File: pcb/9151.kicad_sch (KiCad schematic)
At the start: 17 parts, among them J1 SIM_Card, J5 Conn_ARM_SWD_TagConnect_TC203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, U1 nRF9151-LAXX, U3 W25Q128JVP

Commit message: Clean up sch
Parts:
- removed L1: L_Ferrite, symbol Device:L_Ferrite
- added C38: 0.1u, symbol Device:C
- added FB1: FerriteBead, symbol Device:FerriteBead
- added J9: Conn_Coaxial, symbol Connector:Conn_Coaxial
- added R7, R8: 10k, symbol Device:R
- C1, C2, C5, C6: value C -> 0.1u
- C3: value C -> 15p
- C4: value C -> 47u
- C7, C8: value C -> 4.7u
- R1: value R -> 10k
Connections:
- net +3V3: now also R7.1, R8.1; no longer R1.1
- net GND: now also C38.2, J9.2 (Ext)
- net SCL: now also R7.2
- net SDA: now also R8.2
- net SIM_1V8: now also C38.1
- net V_9151: now also C3.1, FB1.1
- net at C2.1, U1.14 (VDD): now also R1.1, FB1.2; no longer C3.1
- net RF: now reaches U1.35 (ANT)
- net RF: now also J9.1 (In)
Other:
- note added: "Flash"
- note added: "I2C"
- note added: "SWD"
- note added: "TODO: Can internal pullups do this?"
- note added: "nRF9151"
- moved on the sheet: C1, C2, C25, C3, C4, C6, C7, C8, J1, J5, R1, R5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

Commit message: Footprints
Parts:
- C1, C2, C25, C3, C38, C5, C6: footprint (none) -> Capacitor_SMD:C_0603_1608Metric
- C4, C7, C8: footprint (none) -> Capacitor_SMD:C_0805_2012Metric
- FB1: footprint (none) -> Inductor_SMD:L_0603_1608Metric
- J1: footprint (none) -> Connector_Card:nanoSIM_GCT_SIM8060-6-0-14-00
- J9: footprint (none) -> Connector_Coaxial:U.FL_Molex_MCRF_73412-0110_Vertical
- R1, R5, R6, R7, R8: footprint (none) -> Resistor_SMD:R_0603_1608Metric
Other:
- note added: "Internal pull-ups are good to 100kHz"
- note removed: "TODO: Can internal pullups do this?"
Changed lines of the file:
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@@
 		)
 	)
-	(text "Flash"
+	(text "Internal pull-ups \nare good to 100kHz"
 		(exclude_from_sim no)
-		(at 239.014 16.764 0)
+		(at 203.708 151.13 0)
 		(effects
 			(font
-				(size 1.778 1.778)
-				(thickness 0.254)
-				(bold yes)
-				(color 0 11 255 1)
+				(size 1.27 1.27)
+				(color 3 0 255 1)
 			)
 		)
 	)
-	(text "TODO: Can internal \npullups do this?"
+	(text "Flash"
 		(exclude_from_sim no)
-		(at 200.914 150.622 0)
+		(at 239.014 16.764 0)
 		(effects
 			(font
-				(size 1.27 1.27)
+				(size 1.778 1.778)
 				(thickness 0.254)
 				(bold yes)
-				(color 255 0 248 1)
+				(color 0 11 255 1)
 			)
 		)
@@
 			(font
 				(size 1.27 1.27)
-				(color 255 0 235 1)
+				(color 7 0 255 1)
 			)
 		)
@@
 			)
 		)
-		(property "Footprint" ""
+		(property "Footprint" "Capacitor_SMD:C_0603_1608Metric"
 			(at 155.9052 163.83 0)
 			(effects
@@
 			)
 		)
-		(property "Footprint" ""
+		(property "Footprint" "Resistor_SMD:R_0603_1608Metric"
 			(at 212.852 135.89 90)
 			(effects
@@
 			)
 		)
-		(property "Footprint" ""
+		(property "Footprint" "Capacitor_SMD:C_0805_2012Metric"
 			(at 141.9352 35.56 0)
 			(effects
@@
 			)
 		)
-		(property "Footprint" ""
+		(property "Footprint" "Capacitor_SMD:C_0603_1608Metric"
 			(at 254.9652 54.61 0)
 			(effects
@@
 			)
 		)
-		(property "Footprint" ""
+		(property "Footprint" "Capacitor_SMD:C_0603_1608Metric"
 			(at 116.5352 38.1 0)
 			(effects
@@
 			)
 		)
-		(property "Footprint" ""
+		(property "Footprint" "Capacitor_SMD:C_0805_2012Metric"
 			(at 141.9352 64.77 0)
 			(effects
@@
 			)
 		)
-		(property "Footprint" ""
+		(property "Footprint" "Inductor_SMD:L_0603_1608Metric"
 			(at 67.31 28.448 90)
 			(effects
@@
 			)
 		)
-		(property "Footprint" ""
+		(property "Footprint" "Resistor_SMD:R_0603_1608Metric"
 			(at 193.802 135.89 90)
 			(effects
@@
 			)
 		)
-		(property "Footprint" ""
+		(property "Footprint" "Capacitor_SMD:C_0603_1608Metric"
 			(at 91.1352 35.56 0)
 			(effects
@@
 			)
 		)
-		(property "Footprint" ""
+		(property "Footprint" "Resistor_SMD:R_0603_1608Metric"
 			(at 73.152 33.02 90)
 			(effects
@@
 			)
 		)
-		(property "Footprint" ""
+		(property "Footprint" "Resistor_SMD:R_0603_1608Metric"
 			(at 205.232 46.99 90)
 			(effects
@@
 			)
 		)
-		(property "Footprint" ""
+		(property "Footprint" "Connector_Card:nanoSIM_GCT_SIM8060-6-0-14-00"
 			(at 41.91 165.1 0)
 			(effects
@@
 			)
 		)
-		(property "Footprint" ""
+		(property "Footprint" "Capacitor_SMD:C_0603_1608Metric"
 			(at 59.3852 35.56 0)
 			(effects
@@
 			)
 		)
-		(property "Footprint" ""
+		(property "Footprint" "Capacitor_SMD:C_0805_2012Metric"
 			(at 35.2552 35.56 0)
 			(effects
@@
 			)
 		)
-		(property "Footprint" ""
+		(property "Footprint" "Capacitor_SMD:C_0603_1608Metric"
 			(at 46.6852 35.56 0)
 			(effects
@@
 			)
 		)
-		(property "Footprint" ""
+		(property "Footprint" "Resistor_SMD:R_0603_1608Metric"
 			(at 209.042 46.99 90)
 			(effects
@@
 			)
 		)
-		(property "Footprint" ""
+		(property "Footprint" "Capacitor_SMD:C_0603_1608Metric"
 			(at 130.5052 35.56 0)
 			(effects
@@
 			)
 		)
-		(property "Footprint" ""
+		(property "Footprint" "Connector_Coaxial:U.FL_Molex_MCRF_73412-0110_Vertical"
 			(at 151.13 76.2 0)
 			(effects

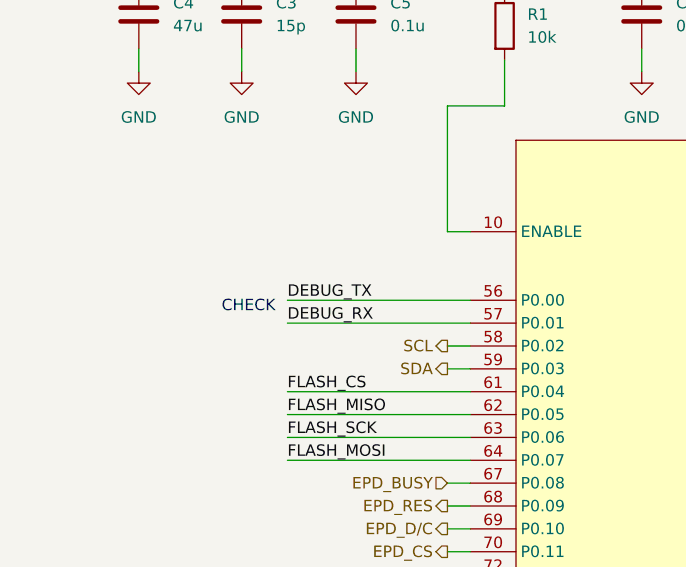
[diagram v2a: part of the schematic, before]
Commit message: ERC errors
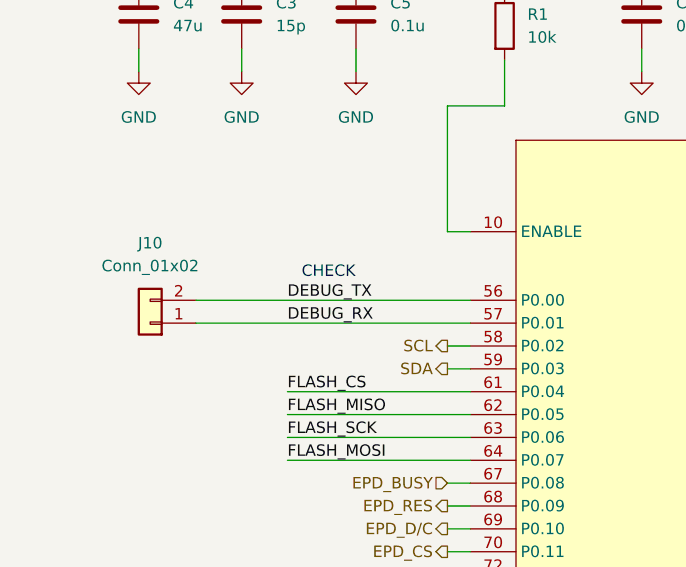
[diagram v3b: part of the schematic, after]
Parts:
- added J10: Conn_01x02, symbol Connector_Generic:Conn_01x02
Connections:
- net DEBUG_RX: now also J10.1 (Pin_1)
- net DEBUG_TX: now also J10.2 (Pin_2)
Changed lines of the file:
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@@
 	(text "CHECK"
 		(exclude_from_sim no)
-		(at 46.482 64.262 0)
+		(at 55.372 60.452 0)
 		(effects
 			(font
@@
 	(wire
 		(pts
-			(xy 50.8 63.5) (xy 71.12 63.5)
+			(xy 207.01 62.23) (xy 228.6 62.23)
 		)
 		(stroke
@@
 	(wire
 		(pts
-			(xy 207.01 62.23) (xy 228.6 62.23)
+			(xy 58.42 35.56) (xy 58.42 38.1)
 		)
 		(stroke
@@
 	(wire
 		(pts
-			(xy 68.58 129.54) (xy 71.12 129.54)
+			(xy 40.64 66.04) (xy 71.12 66.04)
 		)
 		(stroke
@@
 	(wire
 		(pts
-			(xy 256.54 146.05) (xy 256.54 148.59)
+			(xy 40.64 63.5) (xy 71.12 63.5)
 		)
 		(stroke
@@
 	(wire
 		(pts
-			(xy 137.16 154.94) (xy 154.94 154.94)
+			(xy 68.58 129.54) (xy 71.12 129.54)
 		)
 		(stroke
@@
 	(wire
 		(pts
-			(xy 74.93 26.67) (xy 90.17 26.67)
+			(xy 256.54 146.05) (xy 256.54 148.59)
 		)
 		(stroke
@@
 	(wire
 		(pts
-			(xy 256.54 118.11) (xy 256.54 125.73)
+			(xy 137.16 154.94) (xy 154.94 154.94)
 		)
 		(stroke
@@
 	(wire
 		(pts
-			(xy 266.7 138.43) (xy 274.32 138.43)
+			(xy 74.93 26.67) (xy 90.17 26.67)
 		)
 		(stroke
@@
 	(wire
 		(pts
-			(xy 140.97 64.77) (xy 140.97 66.04)
+			(xy 256.54 118.11) (xy 256.54 125.73)
 		)
 		(stroke
@@
 	(wire
 		(pts
-			(xy 34.29 35.56) (xy 34.29 38.1)
+			(xy 266.7 138.43) (xy 274.32 138.43)
 		)
 		(stroke
@@
 	(wire
 		(pts
-			(xy 137.16 160.02) (xy 144.78 160.02)
+			(xy 140.97 64.77) (xy 140.97 66.04)
 		)
 		(stroke
@@
 	(wire
 		(pts
-			(xy 58.42 35.56) (xy 58.42 38.1)
+			(xy 34.29 35.56) (xy 34.29 38.1)
 		)
 		(stroke
@@
 	(wire
 		(pts
-			(xy 50.8 66.04) (xy 71.12 66.04)
+			(xy 137.16 160.02) (xy 144.78 160.02)
 		)
 		(stroke
@@
 					(unit 1)
 				)
+			)
+		)
+	)
+	(symbol
+		(lib_id "Connector_Generic:Conn_01x02")
+		(at 35.56 66.04 180)
+		(unit 1)
+		(exclude_from_sim no)
+		(in_bom yes)
+		(on_board yes)
+		(dnp no)
+		(fields_autoplaced yes)
+		(property "Reference" "J10"
+			(at 35.56 57.15 0)
+			(effects
+				(font
+					(size 1.27 1.27)
+				)
+			)
+		)
+		(property "Value" "Conn_01x02"
+			(at 35.56 59.69 0)
+			(effects
+				(font
+					(size 1.27 1.27)
+				)
+			)
+		)
+		(property "Footprint" ""
+			(at 35.56 66.04 0)
+			(effects
+				(font
+					(size 1.27 1.27)
+				)
+				(hide yes)
+			)
+		)
+		(property "Datasheet" "~"
+			(at 35.56 66.04 0)
+			(effects
+				(font
+					(size 1.27 1.27)
+				)
+				(hide yes)
+			)
+		)
+		(property "Description" "Generic connector, single row, 01x02, script generated (kicad-library-utils/schlib/autogen/connector/)"
+			(at 35.56 66.04 0)
+			(effects
+				(font
+					(size 1.27 1.27)
+				)
+				(hide yes)
+			)
+		)
+		(pin "1"
+		)
+		(pin "2"
+		)
+		(instances
+			(project ""
+				(path "/e4766f3c-98ec-4040-9e57-7309e9dd2214/3c6e67a3-a459-411e-b958-c3a826ee49dc"
+					(reference "J10")
+					(unit 1)
+				)
